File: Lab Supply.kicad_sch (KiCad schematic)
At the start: 48 parts, among them J1 V+, J2 V-, Q1 TIP121, Q2 2N2222, Q3 TIP121, Q4 PNP, Q5 NPN, T1 115V to 24V, U1 LM324, U2 MCP4922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

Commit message: Added DA cinverter
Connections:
- net at C1.2, D5.2 (A), J2.1 (Pin_1)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: now also U1.9 (-)
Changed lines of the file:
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@@
   (junction (at 126.365 153.67) (diameter 0) (color 0 0 0 0)
   )
-  (junction (at 156.845 153.67) (diameter 0) (color 0 0 0 0)
-  )
   (junction (at 31.75 58.42) (diameter 0) (color 0 0 0 0)
   )
@@
   (junction (at 45.72 153.67) (diameter 0) (color 0 0 0 0)
   )
+  (junction (at 157.48 144.78) (diameter 0) (color 0 0 0 0)
+  )
   (junction (at 44.45 30.48) (diameter 0) (color 0 0 0 0)
   )
@@
     (stroke (width 0) (type default))
   )
-  (wire (pts (xy 142.24 153.67) (xy 156.845 153.67))
-    (stroke (width 0) (type default))
-  )
   (wire (pts (xy 44.45 30.48) (xy 44.45 40.64))
     (stroke (width 0) (type default))
@@
     (stroke (width 0) (type default))
   )
-  (wire (pts (xy 156.845 153.67) (xy 181.61 153.67))
+  (wire (pts (xy 142.24 153.67) (xy 181.61 153.67))
     (stroke (width 0) (type default))
   )
@@
     (stroke (width 0) (type default))
   )
+  (wire (pts (xy 157.48 109.22) (xy 157.48 144.78))
+    (stroke (width 0) (type default))
+  )
   (wire (pts (xy 90.17 55.88) (xy 90.17 58.42))
     (stroke (width 0) (type default))
@@
     (stroke (width 0) (type default))
   )
+  (wire (pts (xy 157.48 144.78) (xy 196.85 144.78))
+    (stroke (width 0) (type default))
+  )
   (wire (pts (xy 78.74 76.2) (xy 96.52 76.2))
     (stroke (width 0) (type default))
@@
     (stroke (width 0) (type default))
   )
-  (wire (pts (xy 150.495 144.78) (xy 196.85 144.78))
+  (wire (pts (xy 150.495 144.78) (xy 157.48 144.78))
     (stroke (width 0) (type default))
   )
@@
     (stroke (width 0) (type default))
   )
-  (wire (pts (xy 156.845 108.585) (xy 156.845 153.67))
-    (stroke (width 0) (type default))
-  )

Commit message: WIP
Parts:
- removed D10: 1N4001, symbol Device:D
- removed Q4: PNP, symbol Simulation_SPICE:PNP
- added R17: 10k, Resistor_THT:R_Axial_DIN0207_L6.3mm_D2.5mm_P2.54mm_Vertical, symbol Device:R
- added R18: 10k, symbol Device:R
- added RV1, RV2: 100, symbol Device:R_Potentiometer
- added RV3: 22k, symbol Device:R_Potentiometer
- added RV4: 10k, symbol Device:R_Potentiometer
- added RV6: 20k, symbol Device:R_Potentiometer
- added unit 1 of U1
- added unit 4 of U4
- added U6: MCP3202, symbol Analog_ADC:MCP3202
- added V2, V3: 4.096, symbol Simulation_SPICE:VDC
- D11: footprint (none) -> Diode_THT:D_DO-41_SOD81_P10.16mm_Horizontal
- Q2: value 2N2222 -> 2N3904
- Q5: value NPN -> 2N3904; footprint (none) -> Package_TO_SOT_THT:TO-92_HandSolder
- R1: value 1k -> 10k; footprint (none) -> Resistor_THT:R_Axial_DIN0207_L6.3mm_D2.5mm_P2.54mm_Vertical
- R14: value 47k -> 22k
- R15: value 15k -> 10k; footprint (none) -> Resistor_THT:R_Axial_DIN0207_L6.3mm_D2.5mm_P2.54mm_Vertical
- R16: value 4.7k -> 100k
- R2: footprint (none) -> Resistor_THT:R_Axial_DIN0207_L6.3mm_D2.5mm_P2.54mm_Vertical
- R4: value 39k -> 68k
- R5: value 47k -> 10k; footprint Resistor_THT:R_Axial_DIN0207_L6.3mm_D2.5mm_P2.54mm_Vertical -> (none)
- RLOAD1: value 100 -> 100k
- RV5: value 10k -> 200k; footprint (none) -> Resistor_THT:R_Axial_DIN0207_L6.3mm_D2.5mm_P2.54mm_Vertical
- U2: footprint (none) -> Package_DIP:DIP-14_W7.62mm
- V1: now left out of the parts list
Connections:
- net +28V: now also R1.1
- net GND: now also R5.2, R18.2, RV1.3, RV2.3, RV3.3, U6.4 (VSS), V2.2, V3.2; no longer R15.2
- net at D2.1 (K), U1.8: now also U1.2 (-); no longer R16.2
- net at D11.2 (A), D2.2 (A), Q1.2 (B)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: now also U1.3 (+)
- net V+: now reaches C1.1, D5.1 (K), J1.1 (Pin_1), Q1.3 (E), R4.2, R7.1, RLOAD1.1
- net V+: now also R16.1
- net ISENSE: now reaches C1.2, D5.2 (A), J2.1 (Pin_1), R11.2, R3.1, R6.1, R7.2, RLOAD1.2, U1.9 (-)
- net ISENSE: now also U4.12 (+); no longer R14.2
- net VREF: now reaches R1.2, U2.11 (VrefB), U2.13 (VrefA), U4.2 (A)
- net VREF: now also U6.8 (VDD/VREF)
- net at R5.1: now also RV6.2, U4.13 (-); no longer U1.12 (+)
- net V_VSET: now reaches U2.10 (VB)
- net V_VSET: now also U1.12 (+), RV2.2; no longer R5.2
- net at Q5.2 (B): now also R17.1; no longer R14.1
- net at R15.1, U1.10 (+): now also R2.2
- net V_ISET: now reaches R2.1, U2.14 (VA)
- net V_ISET: now also RV1.2
- net at R4.1: now also RV5.1; no longer RV5.3
- new net: RV2.1, V3.1
- new net: R18.1, RV4.2
- new net: R14.2, U4.14, U6.2 (CH0)
- new net: RV1.1, V2.1
- new net: R16.2, RV4.1, U6.3 (CH1)
- new net: R17.2, U1.1
- new net: R15.2, RV3.2
- new net: R14.1, RV6.1
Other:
- added sheet Controller (untitled.kicad_sch)
- note added: "NOTE: This isn't the true output voltage, since it doesn't take the drop caused by the low side sense into account. But since we collect that drop for the current measurement, we can use it to recover the true output voltage in software."
- moved on the sheet: D3, Q5, R1, R15, R2, R8, RV5, U4

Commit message: Started working on firmware
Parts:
- removed U2: MCP4922, Package_DIP:DIP-14_W7.62mm, symbol Analog_DAC:MCP4922
- removed U3: LM7805, Package_TO_SOT_THT:TO-220-3_Vertical, symbol Regulator_Linear:LM7805_TO220
- removed unit 1 of U4
- added C3: 100n, Capacitor_THT:C_Rect_L10.0mm_W2.5mm_P7.50mm_MKS4, symbol Device:C
- added C8: 100n, symbol Device:C
- added H1: Current, symbol Headers:Rotary_Header
- added H2: Voltage, symbol Headers:Rotary_Header
- added M1: Fan_4pin, symbol Motor:Fan_4pin
- added U2: LM7812_TO220, Package_TO_SOT_THT:TO-220-3_Vertical, symbol Regulator_Linear:LM7812_TO220
- added U3: MCP4922, Package_DIP:DIP-14_W7.62mm, symbol Analog_DAC:MCP4922
- added U4: LM7805_TO220, Package_TO_SOT_THT:TO-220-3_Vertical, symbol Regulator_Linear:LM7805_TO220
- added U5: LM4040DBZ-2.0, Package_TO_SOT_SMD:SOT-23, symbol Reference_Voltage:LM4040DBZ-2.0
- added U7: ~, Arduino:Itsy Bitsy 5V, symbol Arduino:ItsyBitsy_32u4-5V
- R1: value 10k -> 1k
- R14, R16, R18, R5: footprint (none) -> Resistor_THT:R_Axial_DIN0207_L6.3mm_D2.5mm_P2.54mm_Vertical
- RV3, RV4, RV6: footprint (none) -> Potentiometer_THT:Potentiometer_Bourns_3339H_Vertical
- RV5: footprint Resistor_THT:R_Axial_DIN0207_L6.3mm_D2.5mm_P2.54mm_Vertical -> Potentiometer_THT:Potentiometer_Bourns_3339H_Vertical
- U1: renamed from U4; footprint (none) -> Package_DIP:DIP-16_W7.62mm
- U6: footprint (none) -> Package_DIP:DIP-8_W7.62mm
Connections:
- net +28V: now also U2.1 (VI), U4.1 (VI); no longer R1.1
- net GND: now also C3.2, C8.2, H1.1 (GND), H2.1 (GND), U2.2 (GND), U3.12 (Vss), U3.8 (~{LDAC}), U4.2 (GND), U5.1 (K), U7.1 (RST), U7.16 (GND), U7.4 (GND)
- net ISENSE: now also U1.5 (+); no longer U1.12 (+)
- net VREF: now also U3.11 (VrefB), U3.13 (VrefA), U5.2 (A)
- net V_ISET: now also U3.14 (VA)
- net V_VSET: now also U3.10 (VB)
- net at R5.1, RV6.2: now also U1.6 (-); no longer U1.13 (-)
- net at R14.2, U6.2 (CH0): now also U1.7; no longer U1.14
- net at U6.1 (~{CS}/SHDN): now also U7.10 (A5)
- net at U6.5 (DIN): now also U3.5 (SDI), U7.12 (MOSI)
- net at U6.6 (DOUT): now also U7.13 (MISO)
- net at U6.7 (CLK): now also U3.4 (SCK), U7.11 (SCK)
- new net: C8.1, M1.2 (+), U2.3 (VO)
- new net: H1.3 (SW), U7.25 (D9)
- new net: H1.4 (DT), U7.24 (D7)
- new net: H1.5 (CLK), U7.23 (D5)
- new net: H2.5 (CLK), U7.26 (D10)
- new net: H2.4 (DT), U7.27 (D11)
- new net: H2.3 (SW), U7.28 (D12)
- new net +5V: C3.1, H1.2 (+5V), H2.2 (+5V), R1.1, U3.1 (Vdd), U3.9 (~{SHDN}), U4.3 (VO), U7.33 (VBAT)
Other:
- removed sheet Controller
- note added: "IN/~{OUT}"
- moved on the sheet: C1, C2, D11, D2, D3, D5, J1, J2, Q1, Q2, Q5, R10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

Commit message: WIP
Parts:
- added C10, C12, C9: 100n, symbol Device:C
- added C11: 100u, symbol Device:C_Polarized
- added D1, D10, D12, D13, D14: 1N4001, symbol Device:D
- added R19: 10k, symbol Device:R
- R11: value 4.7k -> 10k
- R9: value 4.7k -> 22k
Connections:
- net +36V: now also C12.1
- net GND: now also C10.1, C11.2, C12.2, C9.2
- net VREF: now also D10.1 (K), D12.1 (K)
- net at U3.4 (SCK), U7.11 (SCK): now also D13.2 (A); no longer U6.7 (CLK)
- net at U3.5 (SDI), U7.12 (MOSI): now also D1.2 (A); no longer U6.5 (DIN)
- net at R14.2, U1.7: now also R19.1; no longer U6.2 (CH0)
- net at D9.1 (K), Q3.2 (B), R12.2: now also C11.1
- net at R16.2, RV4.1, U6.3 (CH1): now also C9.1, D12.2 (A)
- net at U6.1 (~{CS}/SHDN): now also D14.1 (K); no longer U7.10 (A5)
- new net: D14.2 (A), U7.10 (A5)
- new net: C10.2, D10.2 (A), R19.2, U6.2 (CH0)
- new net: D13.1 (K), U6.7 (CLK)
- new net: D1.1 (K), U6.5 (DIN)
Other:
- moved on the sheet: C1, C2, D11, D2, D3, D5, D9, J1, J2, Q1, Q2, Q3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

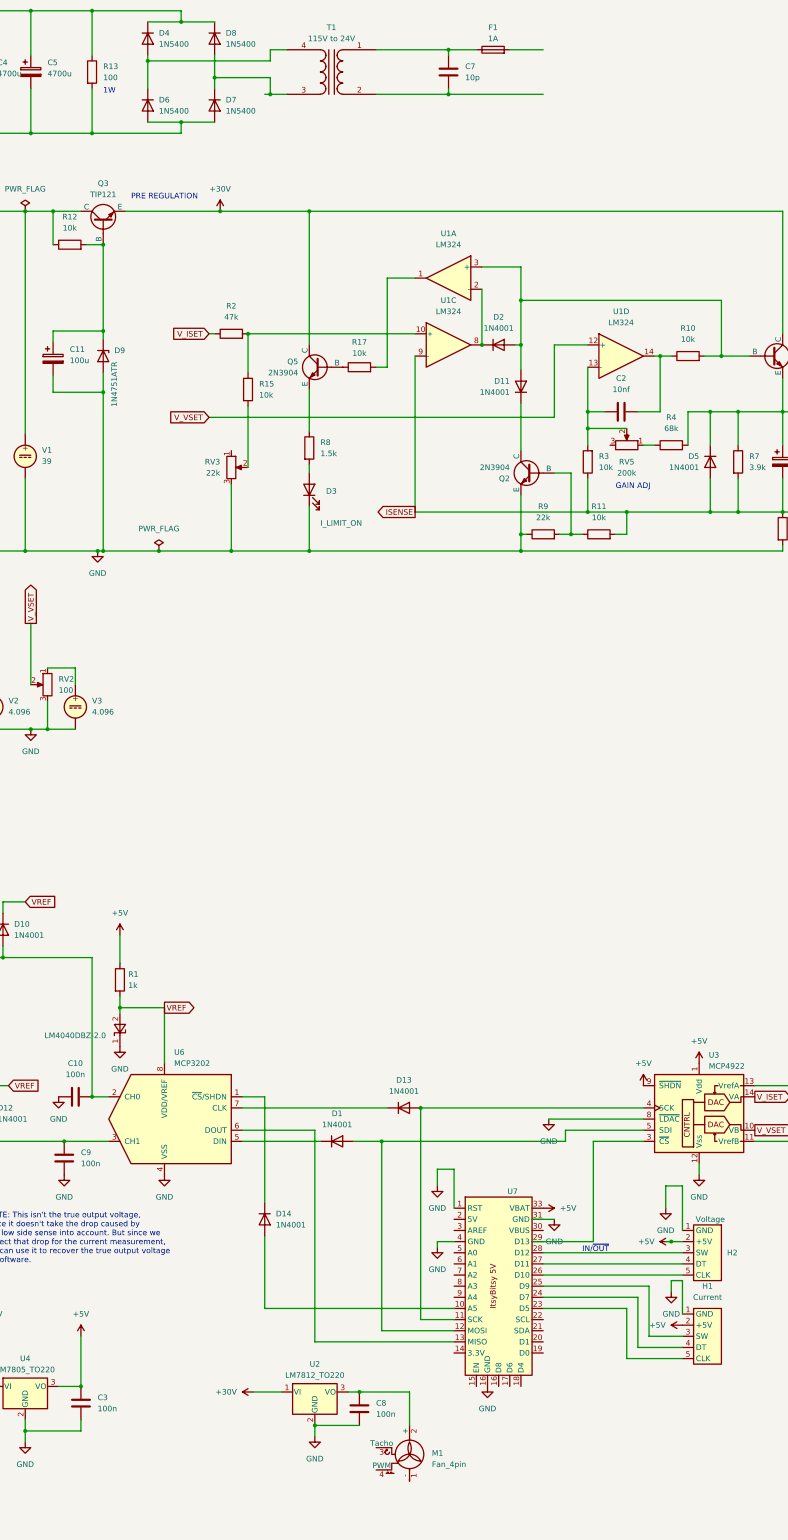
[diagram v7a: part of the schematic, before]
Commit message: Rearranged firmware code
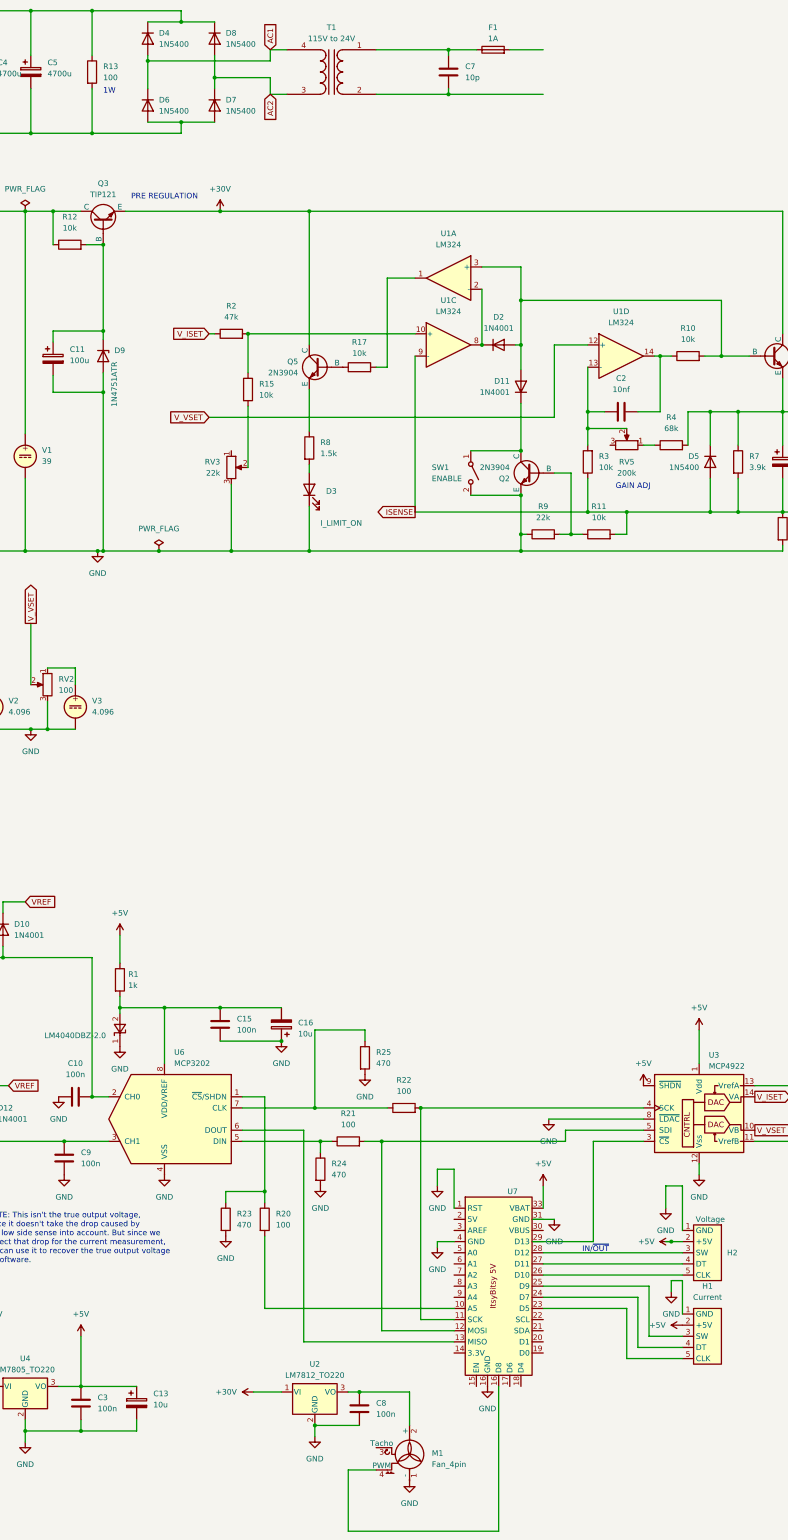
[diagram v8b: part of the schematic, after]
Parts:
- removed D1, D13, D14: 1N4001, symbol Device:D
- added C13, C16: 10u, Capacitor_THT:CP_Radial_D8.0mm_P3.50mm, symbol Device:C_Polarized
- added C15: 100n, Capacitor_THT:C_Rect_L10.0mm_W2.5mm_P7.50mm_MKS4, symbol Device:C
- added R20, R21, R22: 100, Resistor_THT:R_Axial_DIN0204_L3.6mm_D1.6mm_P7.62mm_Horizontal, symbol Device:R
- added R23, R24, R25: 470, Resistor_THT:R_Axial_DIN0204_L3.6mm_D1.6mm_P7.62mm_Horizontal, symbol Device:R
- added SW1: ENABLE, Arduino:2 Pin Header, symbol Switch:SW_SPST
- C10, C12, C8, C9: footprint (none) -> Capacitor_THT:C_Rect_L10.0mm_W2.5mm_P7.50mm_MKS4
- C11: footprint (none) -> Capacitor_THT:CP_Radial_D8.0mm_P3.50mm
- D10, D12: footprint (none) -> Diode_THT:D_DO-41_SOD81_P10.16mm_Horizontal
- D5: value 1N4001 -> 1N5400; footprint Diode_THT:D_DO-41_SOD81_P10.16mm_Horizontal -> Diode_THT:D_DO-201AD_P12.70mm_Horizontal
- D9: footprint Capacitor_THT:CP_Radial_D8.0mm_P3.50mm -> Diode_THT:D_DO-41_SOD81_P10.16mm_Horizontal
- H1: footprint (none) -> Arduino:5 Pin Header
- H2: footprint (none) -> Arduino:5 Pole Header
- M1: footprint (none) -> Connector_Molex:Molex_KK-254_AE-6410-04A_1x04_P2.54mm_Vertical
- Q3: footprint Package_TO_SOT_THT:TO-126-2_Vertical -> Package_TO_SOT_THT:TO-220-3_Vertical
- R1, R10, R11, R12, R13, R14, R15, R16, R17, R18, R2, R3, R4, R5, R7, R8, R9: footprint Resistor_THT:R_Axial_DIN0207_L6.3mm_D2.5mm_P2.54mm_Vertical -> Resistor_THT:R_Axial_DIN0204_L3.6mm_D1.6mm_P7.62mm_Horizontal
- R19: footprint (none) -> Resistor_THT:R_Axial_DIN0204_L3.6mm_D1.6mm_P7.62mm_Horizontal
- R6: footprint Resistor_THT:R_Axial_DIN0207_L6.3mm_D2.5mm_P2.54mm_Vertical -> Resistor_THT:R_Axial_Power_L20.0mm_W6.4mm_P25.40mm
- U1: footprint Package_DIP:DIP-16_W7.62mm -> Package_DIP:DIP-14_W7.62mm
- U5: footprint Package_TO_SOT_SMD:SOT-23 -> Package_TO_SOT_THT:TO-92_HandSolder
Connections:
- net +5V: now also C13.1
- net GND: now also M1.1 (-), C13.2, C15.2, C16.1, R23.2, R24.2, R25.2, SW1.2 (B)
- net VREF: no longer R1.2, U5.2 (A), U6.8 (VDD/VREF)
- net at U3.4 (SCK), U7.11 (SCK): now also R22.2
- net at U3.5 (SDI), U7.12 (MOSI): now also R21.2
- net AC2: now reaches D7.1 (K), D8.2 (A), T1.3 (SA)
- net at D11.1 (K), Q2.1 (C): now also SW1.1 (A)
- net at M1.4 (PWM): now also U7.16 (GND)
- net at U6.1 (~{CS}/SHDN): now also R20.1, R23.1
- net at U7.10 (A5): now also R20.2
- net AC1: now reaches D4.2 (A), D6.1 (K), T1.4 (SB)
- net at U6.7 (CLK): now also R22.1, R25.1
- net at U6.5 (DIN): now also R21.1, R24.1
- new net: C15.1, C16.2, R1.2, U5.2 (A), U6.8 (VDD/VREF)
